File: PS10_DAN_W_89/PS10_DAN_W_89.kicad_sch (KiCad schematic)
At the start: 93 parts, among them J1 Conn_01x15_Pin, J100 Sensor_LEM, J2 IDC26, Q1 2 x BUZ11F1, Q2 2 x BUZ11F1, Q3 2 x BUZ11F1, Q4 2 x BUZ11F1, Q5 VN10KM, U1 AD7545, U10 LF353N, U11 LF355N, U12 LM311, U13 LM311, U14 CNX38, U14 OP77, U15 MC14584B, U16 OP77, U4 MC14013B, U5 LM399, U5 MC14013B, U6 MC14011B, U7 MC14584B, U8 OP77, U9 OP77

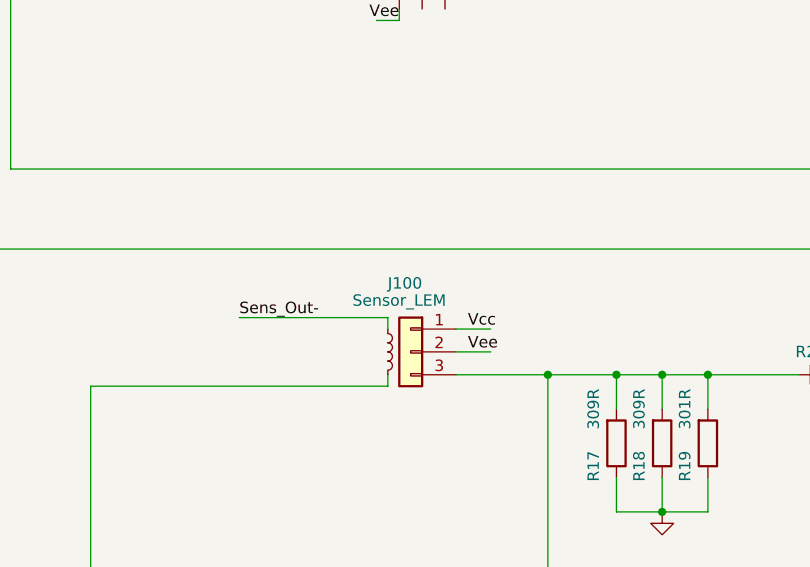
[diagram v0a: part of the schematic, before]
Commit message: The layout of components completed; made corrections in schematics;
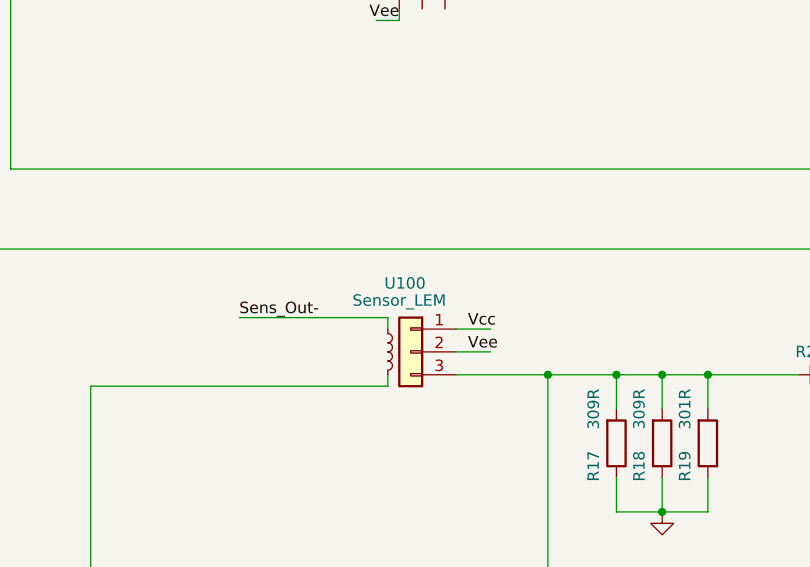
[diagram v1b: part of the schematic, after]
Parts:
- renumbered J100 to U100
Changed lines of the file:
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@@
   (symbol (lib_id "Connector_Generic:Conn_01x03") (at 104.14 152.4 0) (mirror y) (unit 1)
     (in_bom yes) (on_board yes) (dnp no)
-    (property "Reference" "J100" (at 103.505 144.78 0)
+    (property "Reference" "U100" (at 103.505 144.78 0)
       (effects (font (size 1.27 1.27)))
     )
@@
       (project "PS10_DAN_W_89"
         (path "/e91a2aa5-4be5-4ade-bc4c-021deb2b0b30"
-          (reference "J100") (unit 1)
+          (reference "U100") (unit 1)
         )
       )

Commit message: Corrections made (electrical rules check);
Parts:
- added unit 2 of U7
- added unit 5 of U7
- renumbered C7b to C107, C8 to C29, R21b to R121, R21 to R39, U5 to U15, U14 to U17, U15 to U7
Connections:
- net GND: now also J1.10 (Pin_10), J1.11 (Pin_11), J1.2 (Pin_2), J1.4 (Pin_4), J1.9 (Pin_9); no longer J1.12 (Pin_12), J1.14 (Pin_14), J1.5 (Pin_5), J1.6 (Pin_6), J1.7 (Pin_7)
- net Out-: now also J1.7 (Pin_7); no longer J1.9 (Pin_9)
- net SIG1: now also J1.13 (Pin_13); no longer J1.3 (Pin_3)
- net Vcc: now also J1.15 (Pin_15); no longer J1.1 (Pin_1)
- net Vee: now also J1.14 (Pin_14); no longer J1.2 (Pin_2)
- net Vpwr: now also J1.1 (Pin_1), J1.3 (Pin_3); no longer J1.13 (Pin_13), J1.15 (Pin_15)
- net at C1.1, L1.2: now also J1.5 (Pin_5), J1.6 (Pin_6); no longer J1.10 (Pin_10), J1.11 (Pin_11)
- net at U16.2 (-), U16.6: now also J1.12 (Pin_12); no longer J1.4 (Pin_4)
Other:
- moved on the sheet: C18, C19, C20, C21, C22, C23, C24, C25, C26, C27, C28, J2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
